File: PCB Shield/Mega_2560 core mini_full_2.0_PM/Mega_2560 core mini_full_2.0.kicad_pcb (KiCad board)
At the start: 2 copper layers, 89.5 x 59.7 mm, 141 parts, among them P1 2560-core, P10 RX1TX1, P11 Trim, P12 Stick_left, P13 Stick_right, P14 Switch, P15 LCD_I2C, P16 LCD, P17 BATT, P18 Ecolage, P19 Module_TX, P2 Clock, P20 TTL/RS232, P21 Sw_power, P22 JQ6500_28P, P23 Rot_1, P24 Rot_2, P25 Keys, P26 LCD_Alim, P27 HP, P28 5v/3,3v manches, P29 Sw_On, P3 Option, P30 MiniDCDC3A, P31 Pot2, P32 Pot1, P4 Pot3, P5 Vibreur, P6 Micro_sd, P7 SPIX, P8 Audio, P9 SPI, Q1 BSS84, U1 74LVC1G3157GV, U2 TLP290, U3 TLP290, U4 PM5033, U5 LD1117S33TR, U6 MCP604-I/SL, U7 FM24W256, U8 DS3231SN

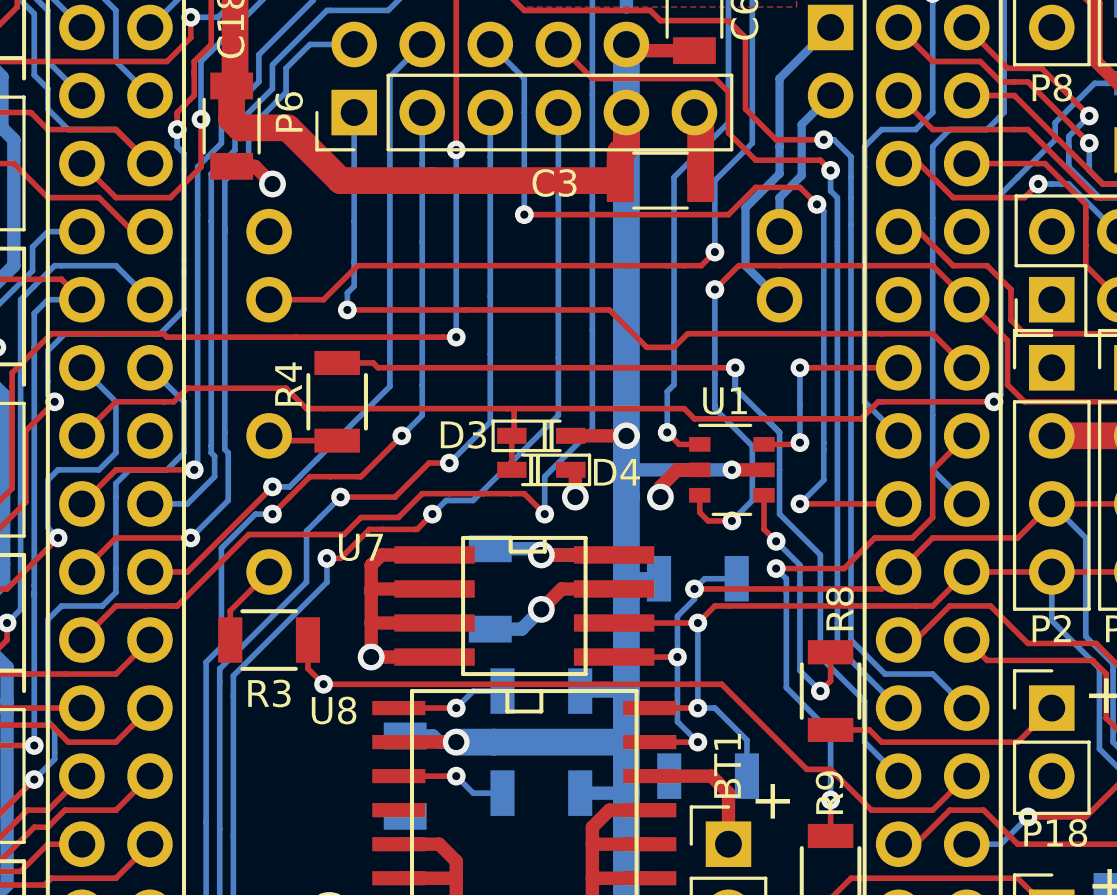
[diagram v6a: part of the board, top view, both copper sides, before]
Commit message: Update shield files before new fabrication
delete two diodes on Vbatt .
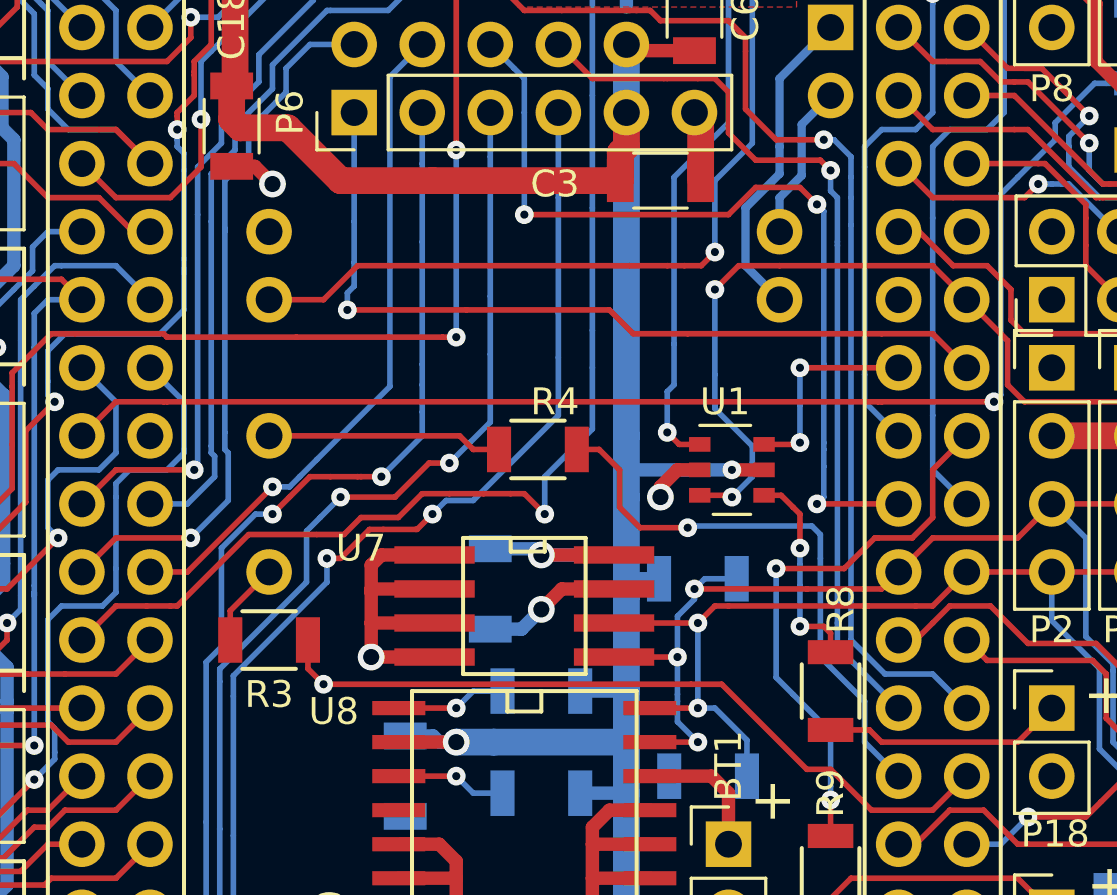
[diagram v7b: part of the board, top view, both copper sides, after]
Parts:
- removed D3, D4: LL4148, MegaCore_Shield:D_SCD80_HandSoldering
- moved R4 7.70 mm to (186.4, 94.1), turned to 180 degrees
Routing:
- net JQ6500Data: track 34.4 -> 21.5 mm
- net Net-(P22-PadRX): track 2.61 -> 9.05 mm
- net U_batt: track 55.4 -> 52.1 mm
- net VCC: track 430.1 -> 428.0 mm, vias 16 -> 15
- net Net-(R8-Pad2): track 9.89 -> 7.88 mm
- net PPM16_SIMout: track 34.2 -> 32.6 mm
- net GND: track 145.7 -> 144.6 mm, vias 21 -> 20
- net Xmitter_SCK: track 33.8 -> 32.9 mm

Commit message: Update silkscreen file
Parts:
- moved C18 2.08 mm to (173.3, 80.8)
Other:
- board text added: "P30"
